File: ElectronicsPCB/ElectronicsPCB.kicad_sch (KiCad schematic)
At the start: 10 parts

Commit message: added power to headers
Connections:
- net +5V: now reaches TAIL.1
- net +5V: now also CAMERA.1, EXTRA3PIN.1, SAIL.1
- net +24V: now reaches VIN.1

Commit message: added rs232 port & stepdown for communication with teensy
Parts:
- ANEMOMETER1: renamed from ANEMOMETER; footprint CONN_B4B-XH-A_JST -> (none)
- EXTRA4PIN1: renamed from EXTRA4PIN; footprint CONN_B4B-XH-A_JST -> (none)
- renumbered 12V to 12V1, CAMERA to CAMERA1, EXTRA3PIN to EXTRA3PIN1, HEADERS to HEADERS1, SAIL to SAIL1, TAIL to TAIL1, TEENSY to TEENSY1, VIN to VIN1
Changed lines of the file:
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@@
 		(dnp no)
 		(fields_autoplaced yes)
-		(property "Reference" "TEENSY"
+		(property "Reference" "TEENSY1"
 			(at 175.26 35.56 0)
 			(effects
@@
 			(project ""
 				(path "/986f98f1-de62-46c2-9c6e-8a3d3d9a8a4d"
-					(reference "TEENSY")
+					(reference "TEENSY1")
 					(unit 1)
 				)
@@
 		(dnp no)
 		(fields_autoplaced yes)
-		(property "Reference" "ANEMOMETER"
+		(property "Reference" "ANEMOMETER1"
 			(at 269.24 101.5999 0)
 			(effects
@@
 			)
 		)
-		(property "Footprint" "CONN_B4B-XH-A_JST"
+		(property "Footprint" ""
 			(at 255.27 99.06 0)
 			(effects
@@
 			(project ""
 				(path "/986f98f1-de62-46c2-9c6e-8a3d3d9a8a4d"
-					(reference "ANEMOMETER")
+					(reference "ANEMOMETER1")
 					(unit 1)
 				)
@@
 		(dnp no)
 		(fields_autoplaced yes)
-		(property "Reference" "TAIL"
+		(property "Reference" "TAIL1"
 			(at 269.24 57.1499 0)
 			(effects
@@
 			(project "ElectronicsPCB"
 				(path "/986f98f1-de62-46c2-9c6e-8a3d3d9a8a4d"
-					(reference "TAIL")
+					(reference "TAIL1")
 					(unit 1)
 				)
@@
 		(dnp no)
 		(fields_autoplaced yes)
-		(property "Reference" "EXTRA4PIN"
+		(property "Reference" "EXTRA4PIN1"
 			(at 269.24 119.3799 0)
 			(effects
@@
 			)
 		)
-		(property "Footprint" "CONN_B4B-XH-A_JST"
+		(property "Footprint" ""
 			(at 255.27 116.84 0)
 			(effects
@@
 			(project "ElectronicsPCB"
 				(path "/986f98f1-de62-46c2-9c6e-8a3d3d9a8a4d"
-					(reference "EXTRA4PIN")
+					(reference "EXTRA4PIN1")
 					(unit 1)
 				)
@@
 		(dnp no)
 		(fields_autoplaced yes)
-		(property "Reference" "CAMERA"
+		(property "Reference" "CAMERA1"
 			(at 269.24 71.1199 0)
 			(effects
@@
 			(project "ElectronicsPCB"
 				(path "/986f98f1-de62-46c2-9c6e-8a3d3d9a8a4d"
-					(reference "CAMERA")
+					(reference "CAMERA1")
 					(unit 1)
 				)
@@
 		(dnp no)
 		(fields_autoplaced yes)
-		(property "Reference" "EXTRA3PIN"
+		(property "Reference" "EXTRA3PIN1"
 			(at 269.24 86.3599 0)
 			(effects
@@
 			(project "ElectronicsPCB"
 				(path "/986f98f1-de62-46c2-9c6e-8a3d3d9a8a4d"
-					(reference "EXTRA3PIN")
+					(reference "EXTRA3PIN1")
 					(unit 1)
 				)
@@
 		(dnp no)
 		(fields_autoplaced yes)
-		(property "Reference" "VIN"
+		(property "Reference" "VIN1"
 			(at 269.24 29.2099 0)
 			(effects
@@
 			(project "ElectronicsPCB"
 				(path "/986f98f1-de62-46c2-9c6e-8a3d3d9a8a4d"
-					(reference "VIN")
+					(reference "VIN1")
 					(unit 1)
 				)
@@
 		(dnp no)
 		(fields_autoplaced yes)
-		(property "Reference" "SAIL"
+		(property "Reference" "SAIL1"
 			(at 269.24 41.9099 0)
 			(effects
@@
 			(project ""
 				(path "/986f98f1-de62-46c2-9c6e-8a3d3d9a8a4d"
-					(reference "SAIL")
+					(reference "SAIL1")
 					(unit 1)
 				)
@@
 		(dnp no)
 		(fields_autoplaced yes)
-		(property "Reference" "12V"
+		(property "Reference" "12V1"
 			(at 269.24 19.0499 0)
 			(effects
@@
 			(project ""
 				(path "/986f98f1-de62-46c2-9c6e-8a3d3d9a8a4d"
-					(reference "12V")
+					(reference "12V1")
 					(unit 1)
 				)
@@
 		(dnp no)
 		(fields_autoplaced yes)
-		(property "Reference" "HEADERS"
+		(property "Reference" "HEADERS1"
 			(at 175.26 93.98 0)
 			(effects
@@
 			(project ""
 				(path "/986f98f1-de62-46c2-9c6e-8a3d3d9a8a4d"
-					(reference "HEADERS")
-					(unit 1)
-				)
+					(reference "HEADERS1")
+					(unit 1)
+				)

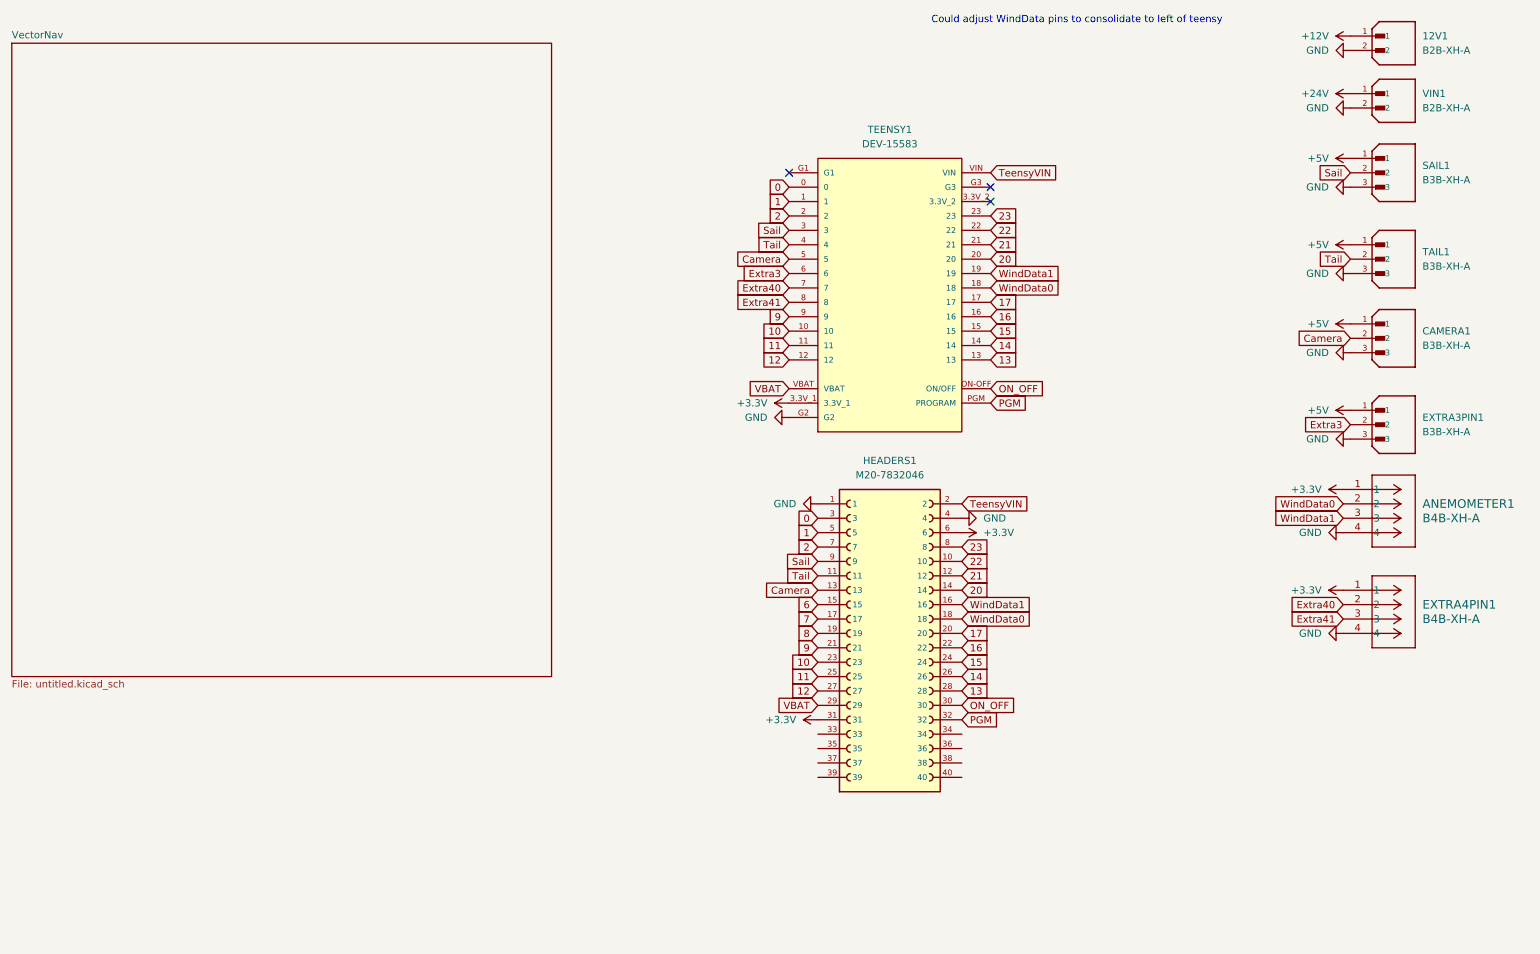
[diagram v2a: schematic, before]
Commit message: updated global label names for vectornav
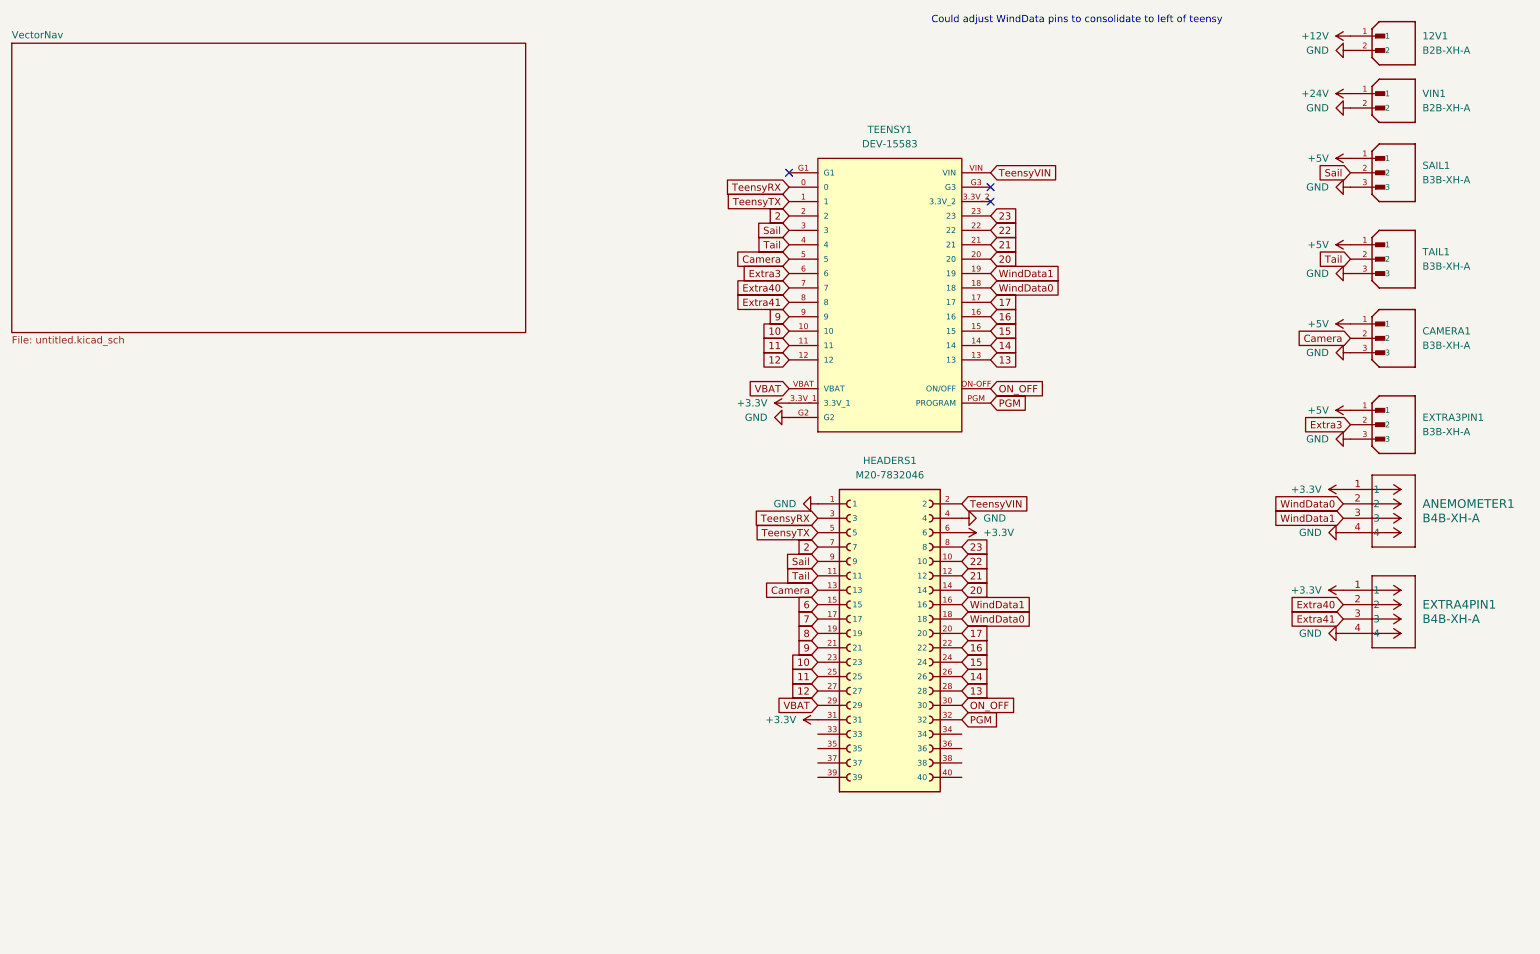
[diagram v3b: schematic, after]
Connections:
- net 0 renamed TeensyRX
- net 1 renamed TeensyTX
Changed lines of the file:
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@@
 		)
 	)
-	(global_label "0"
+	(global_label "TeensyRX"
 		(shape input)
 		(at 162.56 104.14 180)
@@
 		)
 		(property "Intersheetrefs" "${INTERSHEET_REFS}"
-			(at 158.3653 104.14 0)
+			(at 150.8058 104.14 0)
 			(effects
 				(font
@@
 		)
 	)
-	(global_label "1"
+	(global_label "TeensyTX"
 		(shape input)
 		(at 162.56 106.68 180)
@@
 		)
 		(property "Intersheetrefs" "${INTERSHEET_REFS}"
-			(at 158.3653 106.68 0)
+			(at 151.1082 106.68 0)
 			(effects
 				(font
@@
 		)
 	)
-	(global_label "0"
+	(global_label "TeensyRX"
 		(shape input)
 		(at 157.48 45.72 180)
@@
 		)
 		(property "Intersheetrefs" "${INTERSHEET_REFS}"
-			(at 153.2853 45.72 0)
+			(at 145.7258 45.72 0)
 			(effects
 				(font
@@
 		)
 	)
-	(global_label "1"
+	(global_label "TeensyTX"
 		(shape input)
 		(at 157.48 48.26 180)
@@
 		)
 		(property "Intersheetrefs" "${INTERSHEET_REFS}"
-			(at 153.2853 48.26 0)
+			(at 146.0282 48.26 0)
 			(effects
 				(font
@@
 	(sheet
 		(at 20.32 20.32)
-		(size 95.25 111.76)
+		(size 90.678 51.054)
 		(exclude_from_sim no)
 		(in_bom yes)
@@
 		)
 		(property "Sheetfile" "untitled.kicad_sch"
-			(at 20.32 132.6646 0)
+			(at 20.32 71.9586 0)
 			(effects
 				(font

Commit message: added Xbee and merged sheets
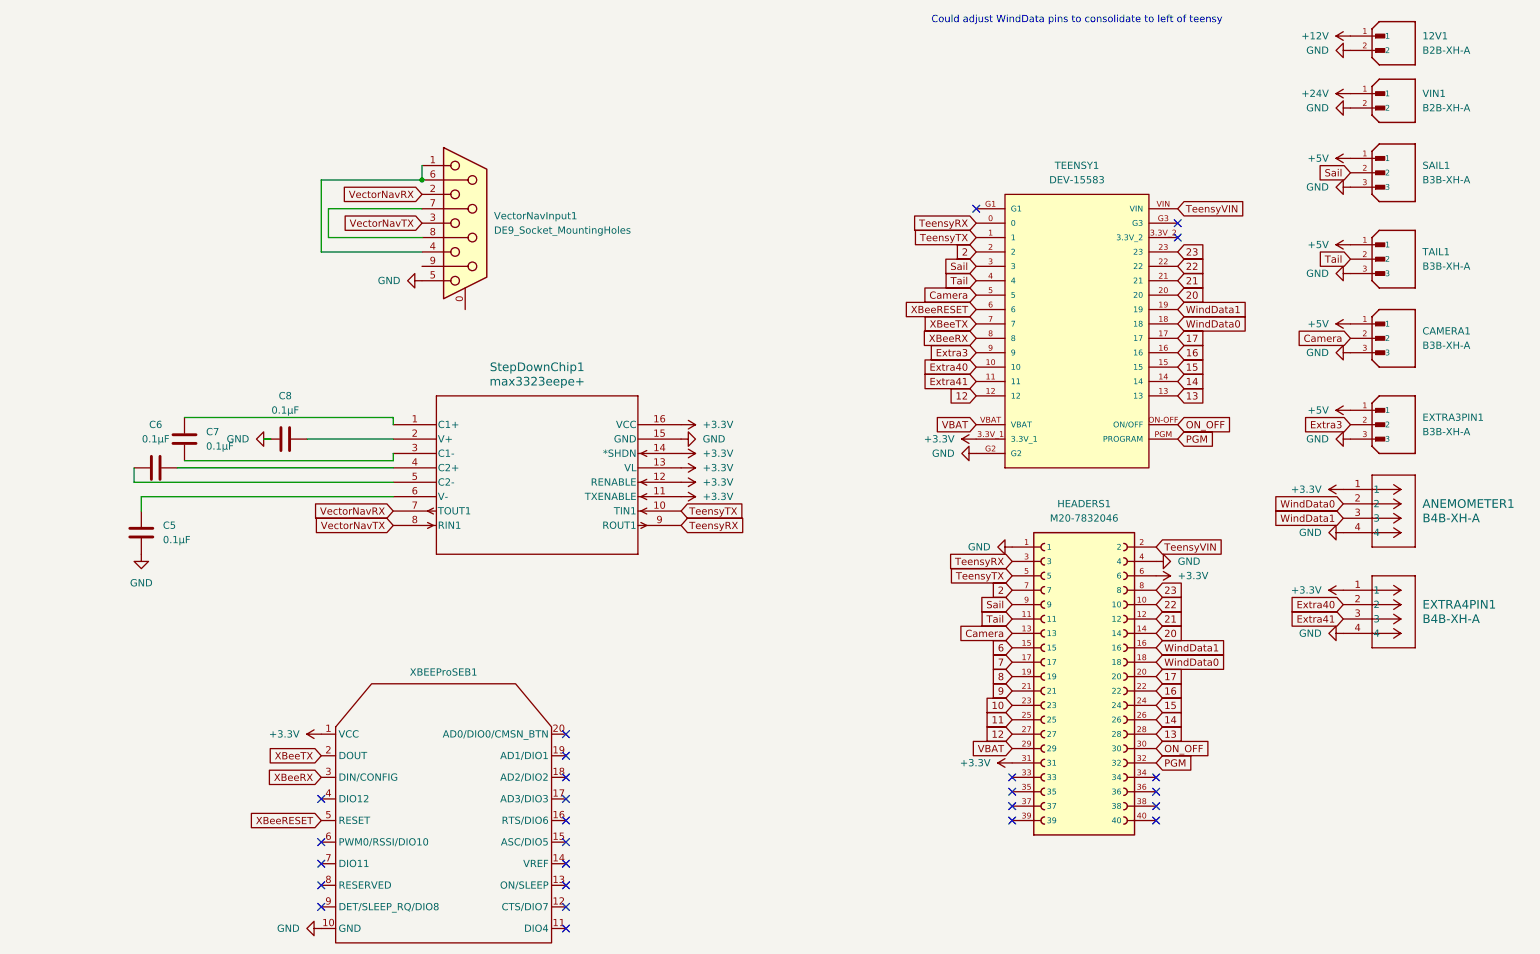
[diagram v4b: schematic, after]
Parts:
- added C5, C6, C7, C8: 0.1µF, symbol Device:C
- added StepDownChip1: max3323eepe+, 21-0043_P16+3_MXM, symbol VectorNav2:max3323eepe+
- added VectorNavInput1: DE9_Socket_MountingHoles, Connector_Dsub:DSUB-9_Socket_Vertical_P2.77x2.84mm_MountingHoles, symbol Connector:DE9_Socket_MountingHoles
- added XBEEProSEB1: ~, symbol VectorNav2:Xbee_pro_s3b
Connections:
- net +3.3V: now also StepDownChip1.11 (TXENABLE), StepDownChip1.12 (RENABLE), StepDownChip1.13 (VL), StepDownChip1.14 (*SHDN), StepDownChip1.16 (VCC), XBEEProSEB1.1 (VCC)
- net 10: no longer TEENSY1.10
- net 11: no longer TEENSY1.11
- net 9: no longer TEENSY1.9
- net Extra3: now also TEENSY1.9; no longer TEENSY1.6
- net Extra40: now also TEENSY1.10; no longer TEENSY1.7
- net Extra41: now also TEENSY1.11; no longer TEENSY1.8
- net GND: now also C5.2, C8.1, StepDownChip1.15 (GND), VectorNavInput1.5, XBEEProSEB1.10 (GND)
- net TeensyRX: now also StepDownChip1.9 (ROUT1)
- net TeensyTX: now also StepDownChip1.10 (TIN1)
- new net: C8.2, StepDownChip1.2 (V+)
- new net: C7.1, StepDownChip1.1 (C1+)
- new net: C7.2, StepDownChip1.3 (C1-)
- new net: C5.1, StepDownChip1.6 (V-)
- new net: VectorNavInput1.1, VectorNavInput1.4, VectorNavInput1.6
- new net: VectorNavInput1.7, VectorNavInput1.8
- new net: C6.1, StepDownChip1.4 (C2+)
- new net: C6.2, StepDownChip1.5 (C2-)
- new net VectorNavRX: StepDownChip1.7 (TOUT1), VectorNavInput1.2
- new net VectorNavTX: StepDownChip1.8 (RIN1), VectorNavInput1.3
- new net XBeeRESET: TEENSY1.6, XBEEProSEB1.5 (RESET)
- new net XBeeRX: TEENSY1.8, XBEEProSEB1.3 (DIN/CONFIG)
- new net XBeeTX: TEENSY1.7, XBEEProSEB1.2 (DOUT)
- no-connect marks 3 -> 26
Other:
- removed sheet VectorNav
- moved on the sheet: HEADERS1, TEENSY1

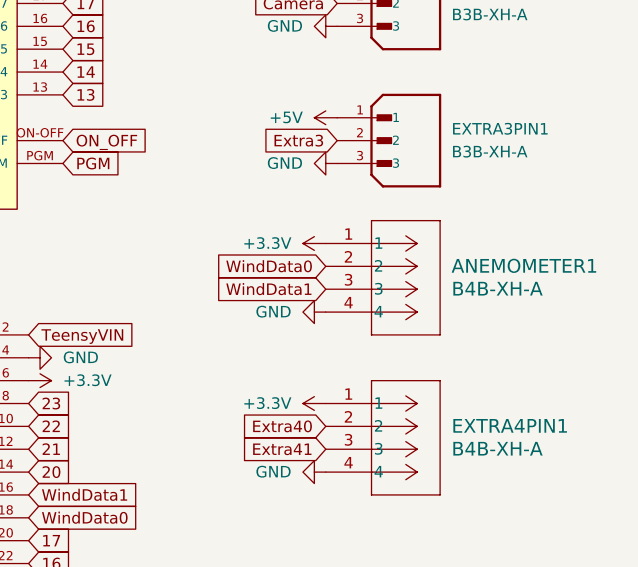
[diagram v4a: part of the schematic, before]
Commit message: assigned footprints
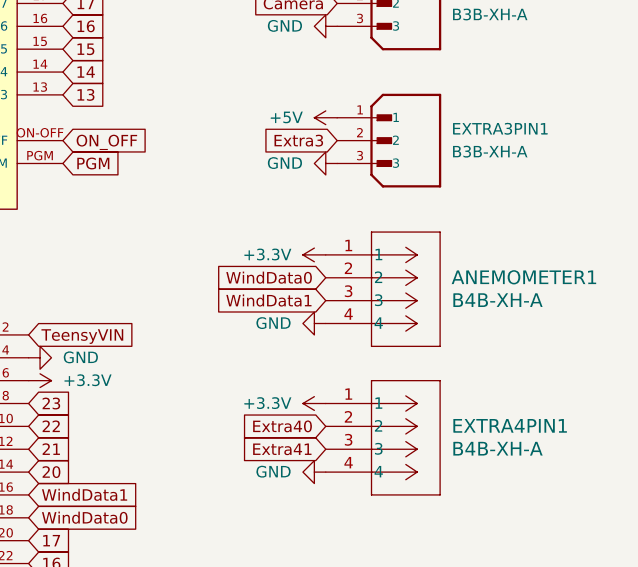
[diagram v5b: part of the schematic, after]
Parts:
- removed ANEMOMETER1, EXTRA4PIN1: B4B-XH-A, symbol 2025-09-13_16-31-34:B4B-XH-A
- added ANEMOMETER1, EXTRA4PIN1: B4B-XH-A, ElectronicsFootprints:B4B-XH-A, symbol 4-PinConnector:B4B-XH-A
- 12V1, VIN1: footprint B2B-XH-A:JST_B2B-XH-A -> ElectronicsFootprints:B2B-XH-A
- C5, C6, C7, C8: footprint (none) -> ElectronicsFootprints:C0402C104K4RACTU_0.1µF
- CAMERA1, EXTRA3PIN1, SAIL1, TAIL1: footprint B3B-XH-A:JST_B3B-XH-A -> ElectronicsFootprints:B3B-XH-A
- HEADERS1: footprint M20-7832046:HARWIN_M20-7832046 -> ElectronicsFootprints:HARWIN_M20-7832046
- StepDownChip1: footprint 21-0043_P16+3_MXM -> ElectronicsFootprints:MAX3323EEPE+
- TEENSY1: footprint DEV-15583:MODULE_DEV-15583 -> ElectronicsFootprints:MODULE_DEV-15583
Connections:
- net +3.3V: now also ANEMOMETER1.1, EXTRA4PIN1.1
- net Extra40: now also EXTRA4PIN1.2
- net Extra41: now also EXTRA4PIN1.3
- net GND: now also ANEMOMETER1.4, EXTRA4PIN1.4
- net WindData0: now also ANEMOMETER1.2
- net WindData1: now also ANEMOMETER1.3

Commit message: started PCB layout, adjusted VIN
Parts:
- removed 12V1: B2B-XH-A, ElectronicsFootprints:B2B-XH-A, symbol 2-PinConnector:B2B-XH-A
- renumbered VIN1 to 5V1, C5 to C1, C6 to C2, C7 to C3, C8 to C4, EXTRA4PIN1 to EXTRA1, EXTRA3PIN1 to EXTRA2, XBEEProSEB1 to XBEE1
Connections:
- net +24V is gone; now on net +5V: 5V1.1

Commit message: added xbee footprint & xbee to layout
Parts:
- XBEE1: footprint (none) -> ElectronicsFootprints:XBee
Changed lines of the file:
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@@
 			)
 		)
-		(property "Footprint" ""
+		(property "Footprint" "ElectronicsFootprints:XBee"
 			(at 96.52 144.78 0)
 			(effects

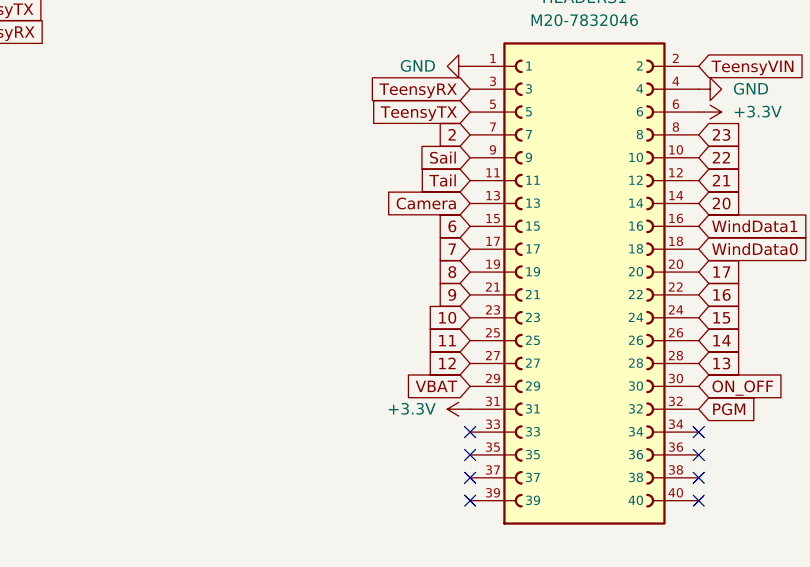
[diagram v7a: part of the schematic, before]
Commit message: began adding traces to layout, updated connections on schematic
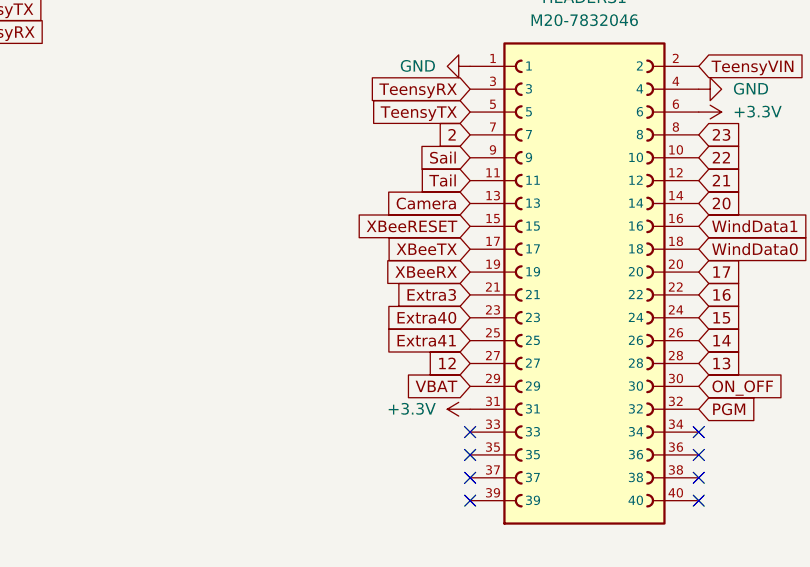
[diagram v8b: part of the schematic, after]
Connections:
- net 10 is gone; now on net Extra40: HEADERS1.23
- net 11 is gone; now on net Extra41: HEADERS1.25
- net 6 is gone; now on net XBeeRESET: HEADERS1.15
- net 7 is gone; now on net XBeeTX: HEADERS1.17
- net 8 is gone; now on net XBeeRX: HEADERS1.19
- net 9 is gone; now on net Extra3: HEADERS1.21
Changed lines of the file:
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@@
 		)
 	)
-	(global_label "10"
+	(global_label "Extra40"
 		(shape input)
 		(at 196.85 137.16 180)
@@
 		)
 		(property "Intersheetrefs" "${INTERSHEET_REFS}"
-			(at 191.4458 137.16 0)
+			(at 186.6078 137.16 0)
 			(effects
 				(font
@@
 		)
 	)
-	(global_label "8"
+	(global_label "XBeeRX"
 		(shape input)
 		(at 196.85 132.08 180)
@@
 		)
 		(property "Intersheetrefs" "${INTERSHEET_REFS}"
-			(at 192.6553 132.08 0)
-			(effects
-				(font
-					(size 1.27 1.27)
-				)
-				(justify right)
-				(hide yes)
-			)
-		)
-	)
-	(global_label "7"
+			(at 186.7286 132.08 0)
+			(effects
+				(font
+					(size 1.27 1.27)
+				)
+				(justify right)
+				(hide yes)
+			)
+		)
+	)
+	(global_label "XBeeTX"
 		(shape input)
 		(at 196.85 129.54 180)
@@
 		)
 		(property "Intersheetrefs" "${INTERSHEET_REFS}"
-			(at 192.6553 129.54 0)
+			(at 187.031 129.54 0)
 			(effects
 				(font
@@
 		)
 	)
-	(global_label "9"
+	(global_label "Extra3"
 		(shape input)
 		(at 196.85 134.62 180)
@@
 		)
 		(property "Intersheetrefs" "${INTERSHEET_REFS}"
-			(at 192.6553 134.62 0)
+			(at 187.8173 134.62 0)
 			(effects
 				(font
@@
 		)
 	)
-	(global_label "11"
+	(global_label "Extra41"
 		(shape input)
 		(at 196.85 139.7 180)
@@
 		)
 		(property "Intersheetrefs" "${INTERSHEET_REFS}"
-			(at 191.4458 139.7 0)
+			(at 186.6078 139.7 0)
 			(effects
 				(font
@@
 		)
 	)
-	(global_label "6"
+	(global_label "XBeeRESET"
 		(shape input)
 		(at 196.85 127 180)
@@
 		)
 		(property "Intersheetrefs" "${INTERSHEET_REFS}"
-			(at 192.6553 127 0)
-			(effects
-				(font
+			(at 183.463 127 0)
+			(effects
+				(font
